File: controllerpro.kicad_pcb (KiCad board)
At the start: 2 copper layers, 92.7 x 78.7 mm, 26 parts, among them P0 Conn_01x08_Male, P1 Conn_01x08_Male, P2 Conn_01x08_Male, P3 Conn_01x08_Male

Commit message: Update boardfile
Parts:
- removed TEENSY2.0: TEENSY_MC_BT_PINS, TEENSY_MC_BT_PINS
- added U1: Teensy2.0, controllerpro:Teensy2.0, F.Cu at (118.1, 105.4)
- PORT1, PORT2, PORT3: footprint controllerpro:NINTENDO-MULTI -> NINTENDO-MULTI
- R1, R10, R4, R7: footprint t32_ref:SOLDERJUMPER -> Capacitors_SMD:C_0603
- R11, R12, R2, R3, R5, R6, R8, R9: footprint t32_ref:SOLDERJUMPER -> Resistors_SMD:R_0805_HandSoldering

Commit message: Fix board
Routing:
- net 5VDATA3: track 23.4 -> 30.2 mm, vias 0 -> 1
- net Net-(U$1-PadRX-I): track 32.9 -> 34.0 mm
- net 3VDATA1: track 66.3 -> 65.3 mm
- net 3VDATA3: track 10.1 -> 9.35 mm
- net Net-(U$1-PadTX-0): track 31.3 -> 31.9 mm

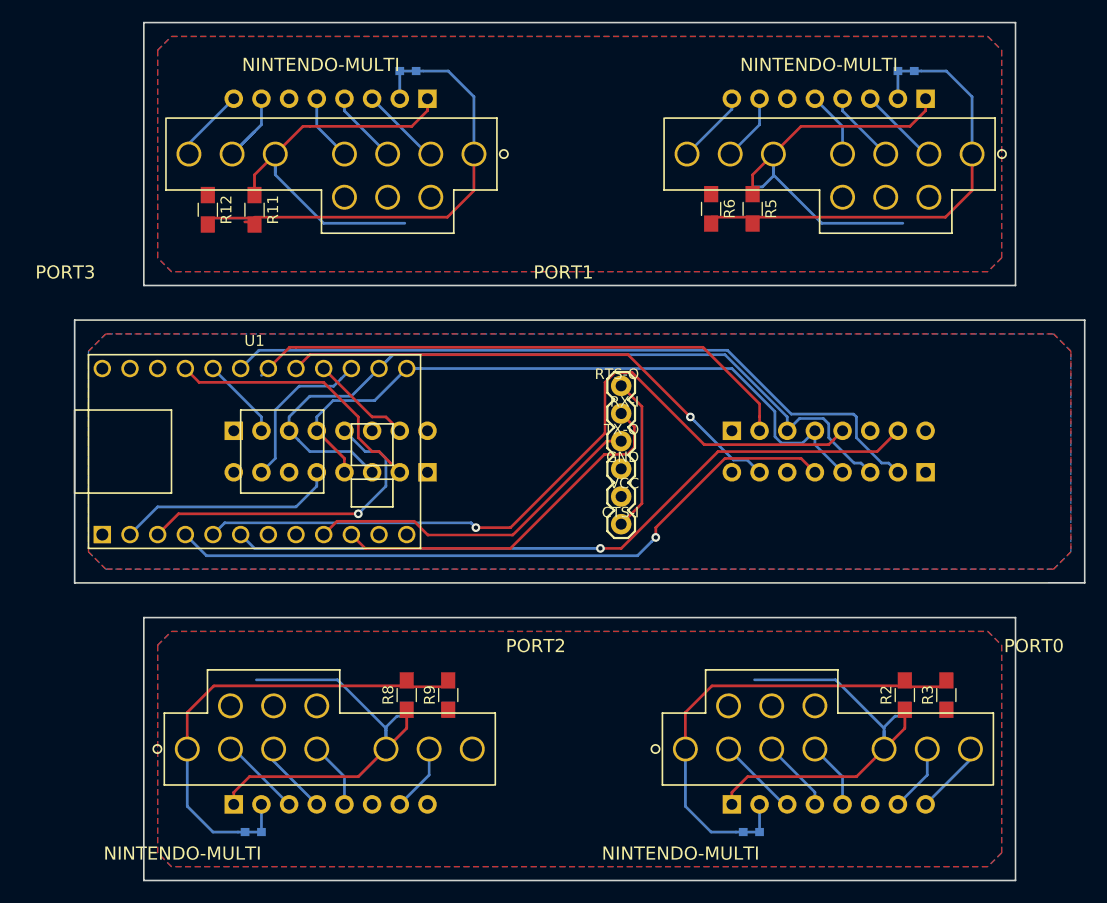
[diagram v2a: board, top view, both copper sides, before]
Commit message: Remove duplicate board, add cutouts
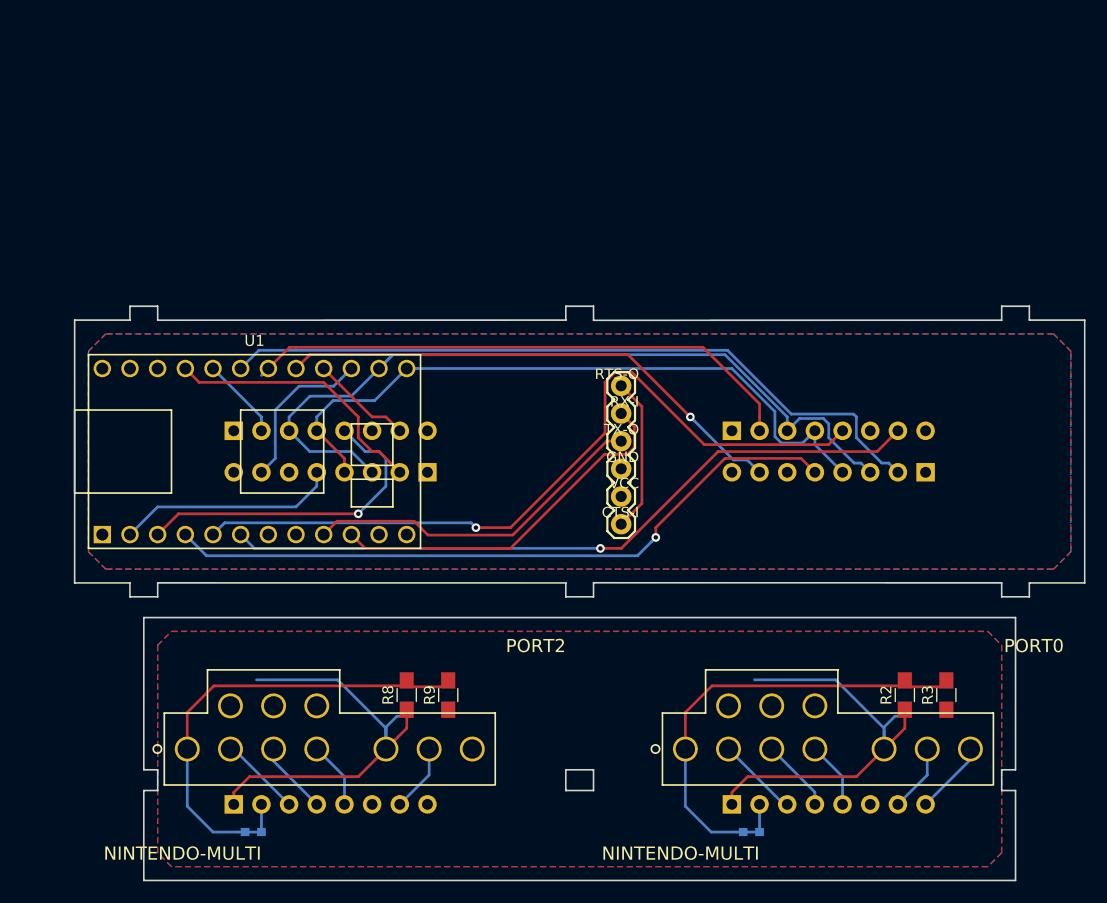
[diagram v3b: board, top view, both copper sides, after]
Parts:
- removed P1, P3: Conn_01x08_Male, Pin_Headers:Pin_Header_Straight_1x08_Pitch2.54mm
- removed PORT1, PORT3: NINTENDO-MULTI, NINTENDO-MULTI
- removed R10, R4: R, Capacitors_SMD:C_0603
- removed R11, R12, R5, R6: R, Resistors_SMD:R_0805_HandSoldering
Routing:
- net VCCB: track 80.9 -> 0.00 mm
- net Net-(P3-Pad2): track 45.3 -> 0.00 mm
- net Net-(P1-Pad2): track 43.9 -> 0.00 mm
- net GNDB: track 14.7 -> 0.00 mm
- net Net-(P3-Pad7): track 9.10 -> 0.00 mm
- net Net-(P3-Pad3): track 7.49 -> 0.00 mm
- net Net-(P1-Pad3): track 7.49 -> 0.00 mm
- net Net-(P3-Pad4): track 7.20 -> 0.00 mm
- net Net-(P1-Pad4): track 6.72 -> 0.00 mm
- net Net-(P1-Pad7): track 6.20 -> 0.00 mm
- net Net-(P1-Pad5): track 6.13 -> 0.00 mm
- net Net-(P3-Pad5): track 6.13 -> 0.00 mm
- removed copper zone on F.Cu, net GNDB
- removed copper zone on B.Cu, net VCCB
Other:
- board size 92.7 x 78.7 mm -> 92.7 x 52.7 mm

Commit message: Remove second board from schematic
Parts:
- PORT0, PORT2: footprint NINTENDO-MULTI -> controllerpro:NINTENDO-MULTI

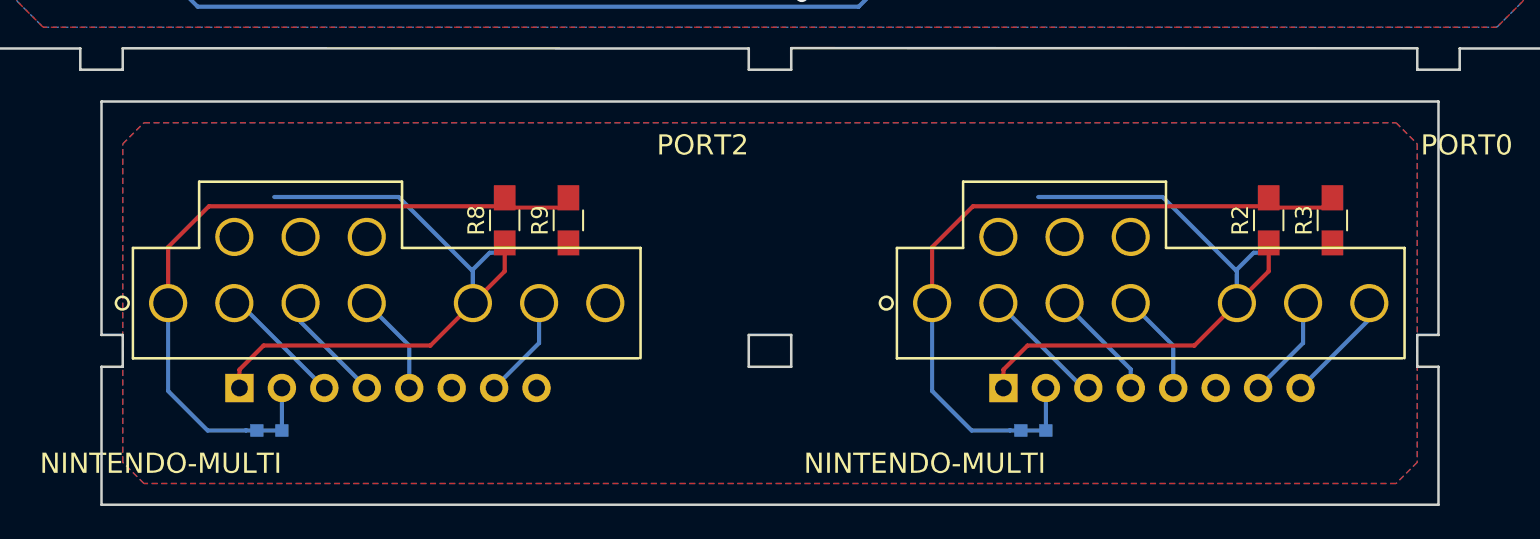
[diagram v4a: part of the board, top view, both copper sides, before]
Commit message: Add pulldown resistors, shrink child board
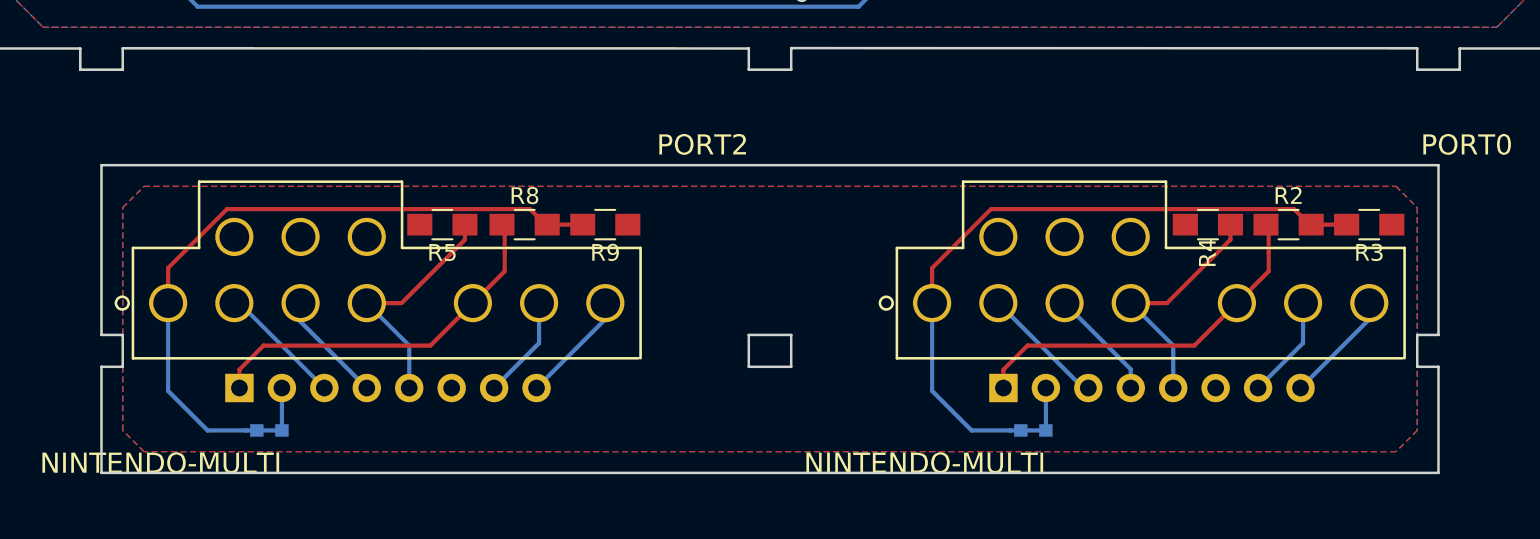
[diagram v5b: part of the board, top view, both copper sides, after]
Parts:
- added R4: R, Resistors_SMD:R_0805_HandSoldering, F.Cu at (174.2, 128.0)
- added R5: R, Resistors_SMD:R_0805_HandSoldering, F.Cu at (128.3, 128.0)
- moved R9 2.22 mm to (138.1, 128.0), turned to 180 degrees
- moved R3 2.22 mm to (183.8, 128.0), turned to 180 degrees
- moved R2 1.22 mm to (179.0, 128.0), turned to 0 degrees
- moved R8 1.22 mm to (133.3, 128.0), turned to 0 degrees
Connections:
- P0 pad 8: GNDA -> Net-(P0-Pad8)
- P2 pad 8: GNDA -> Net-(P2-Pad8)
- PORT0 pad 7: GNDA -> Net-(P0-Pad8)
- PORT2 pad 7: GNDA -> Net-(P2-Pad8)
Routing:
- net VCCA: track 83.0 -> 43.4 mm
- net Net-(P0-Pad5): track 6.13 -> 14.6 mm
- net Net-(P2-Pad5): track 6.13 -> 14.5 mm
- net GNDA: track 7.75 -> 0.00 mm
- net Net-(P2-Pad8): track 0.00 -> 6.78 mm
- net Net-(P0-Pad8): track 0.00 -> 6.78 mm
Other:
- board size 92.7 x 52.7 mm -> 92.7 x 50.8 mm

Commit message: Switch to Teensy 3.2 footprint
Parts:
- U1: value Teensy2.0 -> Teensy3.2; footprint controllerpro:Teensy2.0 -> controllerpro:Teensy30_31_32_LC
- moved U1 2.54 mm to (120.7, 105.4)
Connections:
- U1 pad 2: 5VDATA2 -> 5VDATA1
- U1 pad 22: 3VDATA0 -> LATCH
- U1 pad 23: S_OR_NES1 -> CLOCK
- U1 pad 24: S_OR_NES0 -> 3VDATA2
- U1 pad 25: S_OR_NES3 -> 3VDATA3
- U1 pad 26: S_OR_NES2 -> 3VDATA0
- U1 pad 27: Net-(U1-Pad27) -> S_OR_NES1
- U1 pad 28: Net-(U1-Pad28) -> S_OR_NES0
- U1 pad 29: VCC -> S_OR_NES3
- U1 pad 3: 5VDATA3 -> 5VDATA0
- U1 pad 4: 5VDATA0 -> 5VDATA3
- U1 pad 5: 5VDATA1 -> 5VDATA2
- U1 pad 6: 3VDATA1 -> Net-(U1-Pad6)

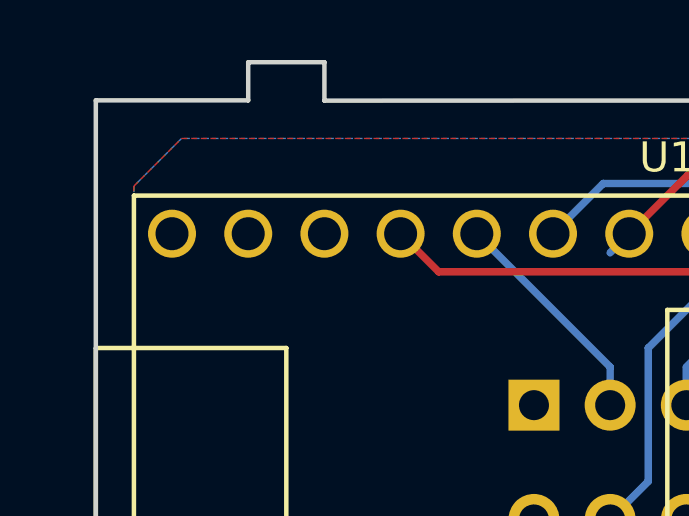
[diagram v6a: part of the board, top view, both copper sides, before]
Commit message: More 3.2 adjustments
Make it Teensy2 compatible even, hopefully!
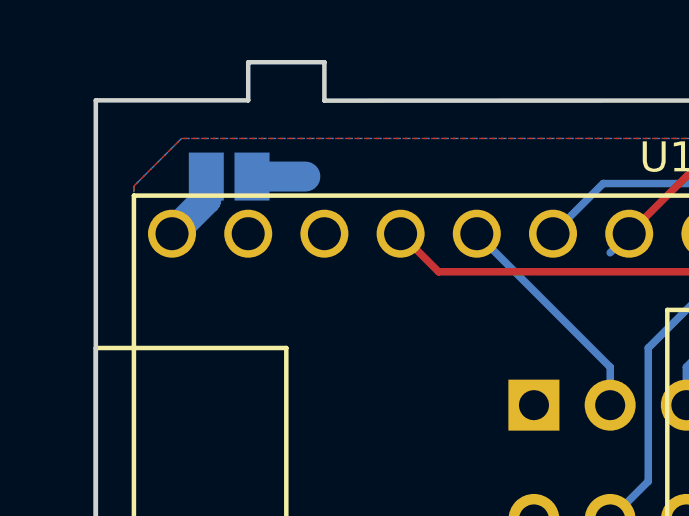
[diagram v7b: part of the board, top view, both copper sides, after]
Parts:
- added JP1: SolderJumper_2_Open, t32_ref:SOLDERJUMPER, B.Cu at (106.0, 95.9)
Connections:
- U1 pad 2: 5VDATA1 -> 5VDATA2
- U1 pad 3: 5VDATA0 -> 5VDATA3
- U1 pad 33: (no net) -> Net-(JP1-Pad2)
- U1 pad 4: 5VDATA3 -> 5VDATA0
- U1 pad 5: 5VDATA2 -> 5VDATA1
- U1 pad 6: Net-(U1-Pad6) -> 3VDATA1
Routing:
- net Net-(JP1-Pad2): track 0.00 -> 2.38 mm
- net VCC: track 0.00 -> 1.78 mm
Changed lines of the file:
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@@
     (thickness 1.6)
     (drawings 82)
-    (tracks 207)
+    (tracks 210)
     (zones 0)
-    (modules 18)
+    (modules 19)
     (nets 50)
   )
@@
   (net 46 "Net-(P0-Pad8)")
   (net 47 "Net-(P2-Pad8)")
-  (net 48 "Net-(U1-Pad6)")
-  (net 49 "Net-(U1-Pad32)")
+  (net 48 "Net-(U1-Pad32)")
+  (net 49 "Net-(JP1-Pad2)")
   (net_class Default "This is the default net class."
     (clearance 0.1524)
@@
     (add_net GNDA)
     (add_net LATCH)
+    (add_net "Net-(JP1-Pad2)")
     (add_net "Net-(P0-Pad2)")
     (add_net "Net-(P0-Pad3)")
@@
     (add_net "Net-(U1-Pad12)")
     (add_net "Net-(U1-Pad32)")
-    (add_net "Net-(U1-Pad6)")
     (add_net "Net-(U1-Pad7)")
     (add_net "Net-(U1-Pad8)")
@@
     (add_net VCC)
     (add_net VCCA)
+  )
+  (module t32_ref:SOLDERJUMPER (layer Bottom)
+    (at 106.045 95.885 180)
+    (fp_text reference JP1 (at 0 0 180) (layer B.Fab)
+      (effects (font (size 0.665 0.665) (thickness 0.056)) (justify left bottom mirror))
+    )
+    (fp_text value SolderJumper_2_Open (at -1.524 -1.651 180) (layer B.SilkS)
+      (effects (font (size 0.38608 0.38608) (thickness 0.04064)) (justify left bottom mirror))
+    )
+    (fp_line (start 1.397 -1.0795) (end -1.397 -1.0795) (layer B.SilkS) (width 0.2032))
+    (fp_arc (start 1.397 0.8255) (end 1.397 1.0795) (angle -90) (layer B.SilkS) (width 0.2032))
+    (fp_arc (start -1.397 0.8255) (end -1.651 0.8255) (angle -90) (layer B.SilkS) (width 0.2032))
+    (fp_arc (start -1.397 -0.8255) (end -1.651 -0.8255) (angle 90) (layer B.SilkS) (width 0.2032))
+    (fp_arc (start 1.397 -0.8255) (end 1.397 -1.0795) (angle 90) (layer B.SilkS) (width 0.2032))
+    (fp_line (start 1.651 -0.8255) (end 1.651 0.8255) (layer B.SilkS) (width 0.2032))
+    (fp_line (start -1.651 -0.8255) (end -1.651 0.8255) (layer B.SilkS) (width 0.2032))
+    (fp_line (start -1.397 1.0795) (end 1.397 1.0795) (layer B.SilkS) (width 0.2032))
+    (fp_poly (pts (xy -0.0762 -0.9144) (xy 0.0762 -0.9144) (xy 0.0762 0.9144) (xy -0.0762 0.9144)) (layer B.Mask) (width 0))
+    (fp_line (start -1.4 0.8) (end 1.4 0.8) (layer B.Fab) (width 0.05))
+    (fp_line (start 1.4 0.8) (end 1.4 -0.8) (layer B.Fab) (width 0.05))
+    (fp_line (start 1.4 -0.8) (end -1.4 -0.8) (layer B.Fab) (width 0.05))
+    (fp_line (start -1.4 -0.8) (end -1.4 0.8) (layer B.Fab) (width 0.05))
+    (pad 1 smd rect (at -0.762 0 180) (size 1.1684 1.6002) (layers Bottom B.Paste B.Mask)
+      (net 3 VCC) (solder_mask_margin 0.1016))
+    (pad 2 smd rect (at 0.762 0 180) (size 1.1684 1.6002) (layers Bottom B.Paste B.Mask)
+      (net 49 "Net-(JP1-Pad2)") (solder_mask_margin 0.1016))
   )
   (module controllerpro:Teensy30_31_32_LC (layer Top)
@@
       (net 3 VCC))
     (pad 32 thru_hole circle (at -13.97 -7.62) (size 1.6 1.6) (drill 1.1) (layers *.Cu *.Mask F.SilkS)
-      (net 49 "Net-(U1-Pad32)"))
-    (pad 33 thru_hole circle (at -16.51 -7.62) (size 1.6 1.6) (drill 1.1) (layers *.Cu *.Mask F.SilkS))
+      (net 48 "Net-(U1-Pad32)"))
+    (pad 33 thru_hole circle (at -16.51 -7.62) (size 1.6 1.6) (drill 1.1) (layers *.Cu *.Mask F.SilkS)
+      (net 49 "Net-(JP1-Pad2)"))
     (pad 12 thru_hole circle (at 11.43 7.62) (size 1.6 1.6) (drill 1.1) (layers *.Cu *.Mask F.SilkS)
       (net 44 "Net-(U1-Pad12)"))
@@
       (net 39 "Net-(U1-Pad7)"))
     (pad 6 thru_hole circle (at -3.81 7.62) (size 1.6 1.6) (drill 1.1) (layers *.Cu *.Mask F.SilkS)
-      (net 48 "Net-(U1-Pad6)"))
+      (net 14 3VDATA1))
     (pad 5 thru_hole circle (at -6.35 7.62) (size 1.6 1.6) (drill 1.1) (layers *.Cu *.Mask F.SilkS)
+      (net 6 5VDATA1))
+    (pad 4 thru_hole circle (at -8.89 7.62) (size 1.6 1.6) (drill 1.1) (layers *.Cu *.Mask F.SilkS)
+      (net 5 5VDATA0))
+    (pad 3 thru_hole circle (at -11.43 7.62) (size 1.6 1.6) (drill 1.1) (layers *.Cu *.Mask F.SilkS)
+      (net 8 5VDATA3))
+    (pad 2 thru_hole circle (at -13.97 7.62) (size 1.6 1.6) (drill 1.1) (layers *.Cu *.Mask F.SilkS)
       (net 7 5VDATA2))
-    (pad 4 thru_hole circle (at -8.89 7.62) (size 1.6 1.6) (drill 1.1) (layers *.Cu *.Mask F.SilkS)
-      (net 8 5VDATA3))
-    (pad 3 thru_hole circle (at -11.43 7.62) (size 1.6 1.6) (drill 1.1) (layers *.Cu *.Mask F.SilkS)
-      (net 5 5VDATA0))
-    (pad 2 thru_hole circle (at -13.97 7.62) (size 1.6 1.6) (drill 1.1) (layers *.Cu *.Mask F.SilkS)
-      (net 6 5VDATA1))
     (pad 1 thru_hole rect (at -16.51 7.62) (size 1.6 1.6) (drill 1.1) (layers *.Cu *.Mask F.SilkS)
       (net 4 GND))
@@
   (segment (start 126.365 107.315) (end 126.365 106.045) (width 0.25) (layer Top) (net 2))
   (segment (start 126.365 106.045) (end 123.825 103.505) (width 0.25) (layer Top) (net 2))
+  (segment (start 106.807 95.885) (end 108.585 95.885) (width 1) (layer Bottom) (net 3))
   (segment (start 161.29 106.045) (end 154.94 112.395) (width 0.25) (layer Top) (net 5))
   (segment (start 154.94 112.395) (end 154.94 113.294701) (width 0.25) (layer Top) (net 5))
@@
   (segment (start 169.545 107.315) (end 168.275 106.045) (width 0.25) (layer Top) (net 5))
   (via (at 154.94 113.294701) (size 0.8) (drill 0.4) (layers Top Bottom) (net 5))
-  (segment (start 114.3 113.03) (end 115.377401 111.952599) (width 0.25) (layer Bottom) (net 6))
-  (segment (start 137.987599 111.952599) (end 138.030001 111.995001) (width 0.25) (layer Bottom) (net 6))
-  (segment (start 138.030001 111.995001) (end 138.43 112.395) (width 0.25) (layer Bottom) (net 6))
   (segment (start 115.377401 111.952599) (end 137.987599 111.952599) (width 0.25) (layer Bottom) (net 6))
+  (segment (start 114.3 113.03) (end 115.377401 111.952599) (width 0.25) (layer Bottom) (net 6) (status 1000000))
+  (segment (start 138.030001 111.995001) (end 138.43 112.395) (width 0.25) (layer Bottom) (net 6) (status 1000000))
+  (segment (start 137.987599 111.952599) (end 138.030001 111.995001) (width 0.25) (layer Bottom) (net 6) (status 1000000))
   (segment (start 151.180743 98.160299) (end 152.770299 98.160299) (width 0.25) (layer Top) (net 6))
-  (segment (start 171.235001 104.354999) (end 172.085 103.505) (width 0.25) (layer Top) (net 6))
-  (segment (start 150.281042 99.06) (end 151.180743 98.160299) (width 0.25) (layer Top) (net 6))
-  (segment (start 150.281042 103.718958) (end 150.281042 99.06) (width 0.25) (layer Top) (net 6))
   (segment (start 141.605 112.395) (end 150.281042 103.718958) (width 0.25) (layer Top) (net 6))
   (via (at 138.43 112.395) (size 0.8) (drill 0.4) (layers Top Bottom) (net 6))
@@
   (segment (start 138.43 112.395) (end 141.605 112.395) (width 0.25) (layer Top) (net 6))
   (segment (start 159.385 104.775) (end 170.815 104.775) (width 0.25) (layer Top) (net 6))
+  (segment (start 150.281042 99.06) (end 151.180743 98.160299) (width 0.25) (layer Top) (net 6))
+  (segment (start 171.235001 104.354999) (end 172.085 103.505) (width 0.25) (layer Top) (net 6))
+  (segment (start 150.281042 103.718958) (end 150.281042 99.06) (width 0.25) (layer Top) (net 6))
   (segment (start 127.635 111.125) (end 111.125 111.125) (width 0.25) (layer Top) (net 8))
   (segment (start 111.125 111.125) (end 109.22 113.03) (width 0.25) (layer Top) (net 8))
@@
   (segment (start 133.985 137.795) (end 138.0998 133.6802) (width 0.25) (layer Bottom) (net 47))
   (segment (start 138.0998 133.6802) (end 138.0998 132.715) (width 0.25) (layer Bottom) (net 47))
+  (segment (start 105.283 95.885) (end 105.283 96.647) (width 1) (layer Bottom) (net 49))
+  (segment (start 105.283 96.647) (end 104.14 97.79) (width 1) (layer Bottom) (net 49))
   (zone (net 4) (net_name GND) (layer Top) (hatch edge 0.508)
     (priority 6)
